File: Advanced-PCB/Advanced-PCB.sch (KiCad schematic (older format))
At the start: 24 parts, among them J1 USB_mini_micro_B, SW1 MXSwitch, SW2 MXSwitch, SW3 MXSwitch, SW4 MXSwitch, U1 ATMEGA32U4, X1 16MHz

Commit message: First Row Added
First Row added to layout and keycaps labeled.
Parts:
- removed D2: D_Small, Diode_SMD:D_SOD-123, symbol Device:D_Small
- removed SW2: MXSwitch, acheron_MXH:MX100H, symbol acheronSymbols:MXSwitch
- added D10, D11, D12, D13, D14, D15, D3, D5, D6, D7, D8, D9: 1N4148W, Diode_SMD:D_SOD-123, symbol Device:D_Small
- added SW10: 9, acheron_MXH:MX100H, symbol acheronSymbols:MXSwitch
- added SW11: 0, acheron_MXH:MX100H, symbol acheronSymbols:MXSwitch
- added SW12: -, acheron_MXH:MX100H, symbol acheronSymbols:MXSwitch
- added SW13: =, acheron_MXH:MX100H, symbol acheronSymbols:MXSwitch
- added SW14: Back, acheron_MXH:MX100H, symbol acheronSymbols:MXSwitch
- added SW15: `, acheron_MXH:MX100H, symbol acheronSymbols:MXSwitch
- added SW3: 2, acheron_MXH:MX100H, symbol acheronSymbols:MXSwitch
- added SW5: 4, acheron_MXH:MX100H, symbol acheronSymbols:MXSwitch
- added SW6: 5, acheron_MXH:MX100H, symbol acheronSymbols:MXSwitch
- added SW7: 6, acheron_MXH:MX100H, symbol acheronSymbols:MXSwitch
- added SW8: 7, acheron_MXH:MX100H, symbol acheronSymbols:MXSwitch
- added SW9: 8, acheron_MXH:MX100H, symbol acheronSymbols:MXSwitch
- D1, D4: value D_Small -> 1N4148W
- D2: renamed from D3; value D_Small -> 1N4148W
- SW1: value MXSwitch -> Esc
- SW2: renamed from SW3; value MXSwitch -> 1
- SW4: value MXSwitch -> 3
- renumbered C3 to C1, C1 to C2, C4 to C3, C5 to C4, C6 to C5, C7 to C6, C2 to C7, R3 to R2, R4 to R3, R2 to R4
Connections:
- net labels added: Col10, Col11, Col12, Col13, Col14, Col15, Col3, Col4, Col5, Col6, Col7, Col8, Col9, Row4, Row5
- net labels removed: Row2
- wire segments 74 -> 146
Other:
- moved on the sheet: C1, C2, C3, C4, C5, C6, C7, C8, J1, R1, R2, R3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

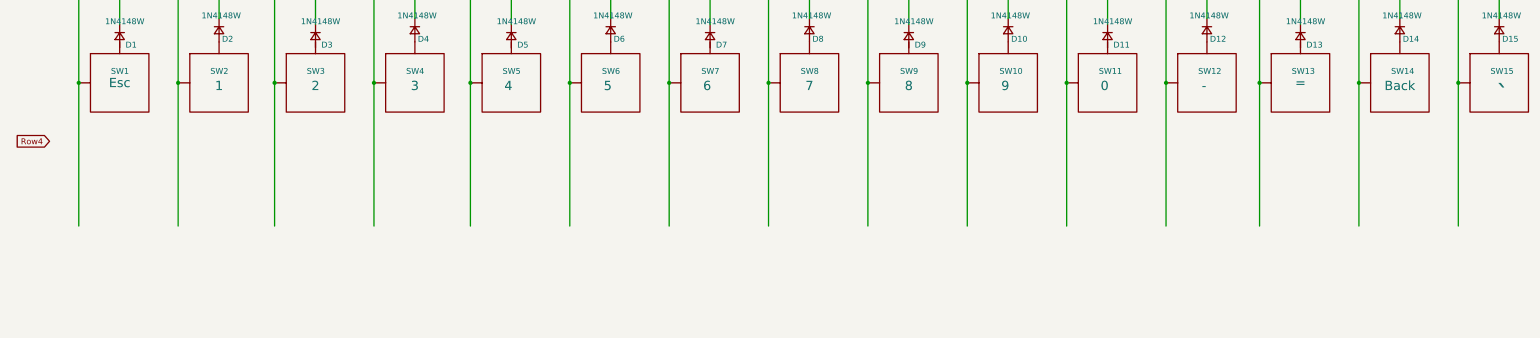
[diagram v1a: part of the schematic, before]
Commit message: Second Row Added
Second Row added to Matrix and Labeled.
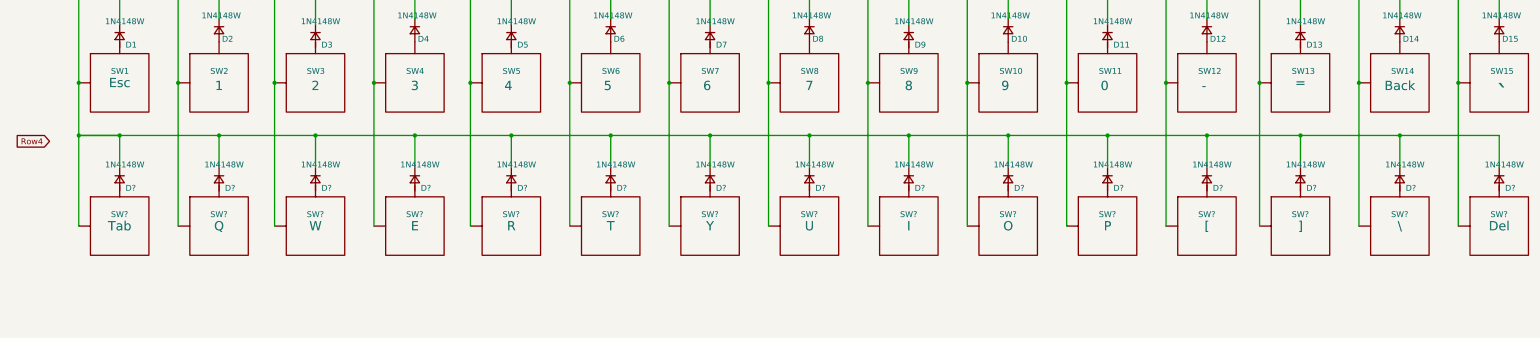
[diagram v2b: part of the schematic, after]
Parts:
- added D? (x15): 1N4148W, Diode_SMD:D_SOD-123, symbol Device:D_Small
- added SW?: Tab, acheron_MXH:MX100H, symbol acheronSymbols:MXSwitch
- added SW?: Q, acheron_MXH:MX100H, symbol acheronSymbols:MXSwitch
- added SW?: W, acheron_MXH:MX100H, symbol acheronSymbols:MXSwitch
- added SW?: E, acheron_MXH:MX100H, symbol acheronSymbols:MXSwitch
- added SW?: R, acheron_MXH:MX100H, symbol acheronSymbols:MXSwitch
- added SW?: T, acheron_MXH:MX100H, symbol acheronSymbols:MXSwitch
- added SW?: Y, acheron_MXH:MX100H, symbol acheronSymbols:MXSwitch
- added SW?: U, acheron_MXH:MX100H, symbol acheronSymbols:MXSwitch
- added SW?: I, acheron_MXH:MX100H, symbol acheronSymbols:MXSwitch
- added SW?: O, acheron_MXH:MX100H, symbol acheronSymbols:MXSwitch
- added SW?: P, acheron_MXH:MX100H, symbol acheronSymbols:MXSwitch
- added SW?: [, acheron_MXH:MX100H, symbol acheronSymbols:MXSwitch
- added SW?: ], acheron_MXH:MX100H, symbol acheronSymbols:MXSwitch
- added SW?: \\, acheron_MXH:MX100H, symbol acheronSymbols:MXSwitch
- added SW?: Del, acheron_MXH:MX100H, symbol acheronSymbols:MXSwitch
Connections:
- wire segments 146 -> 178

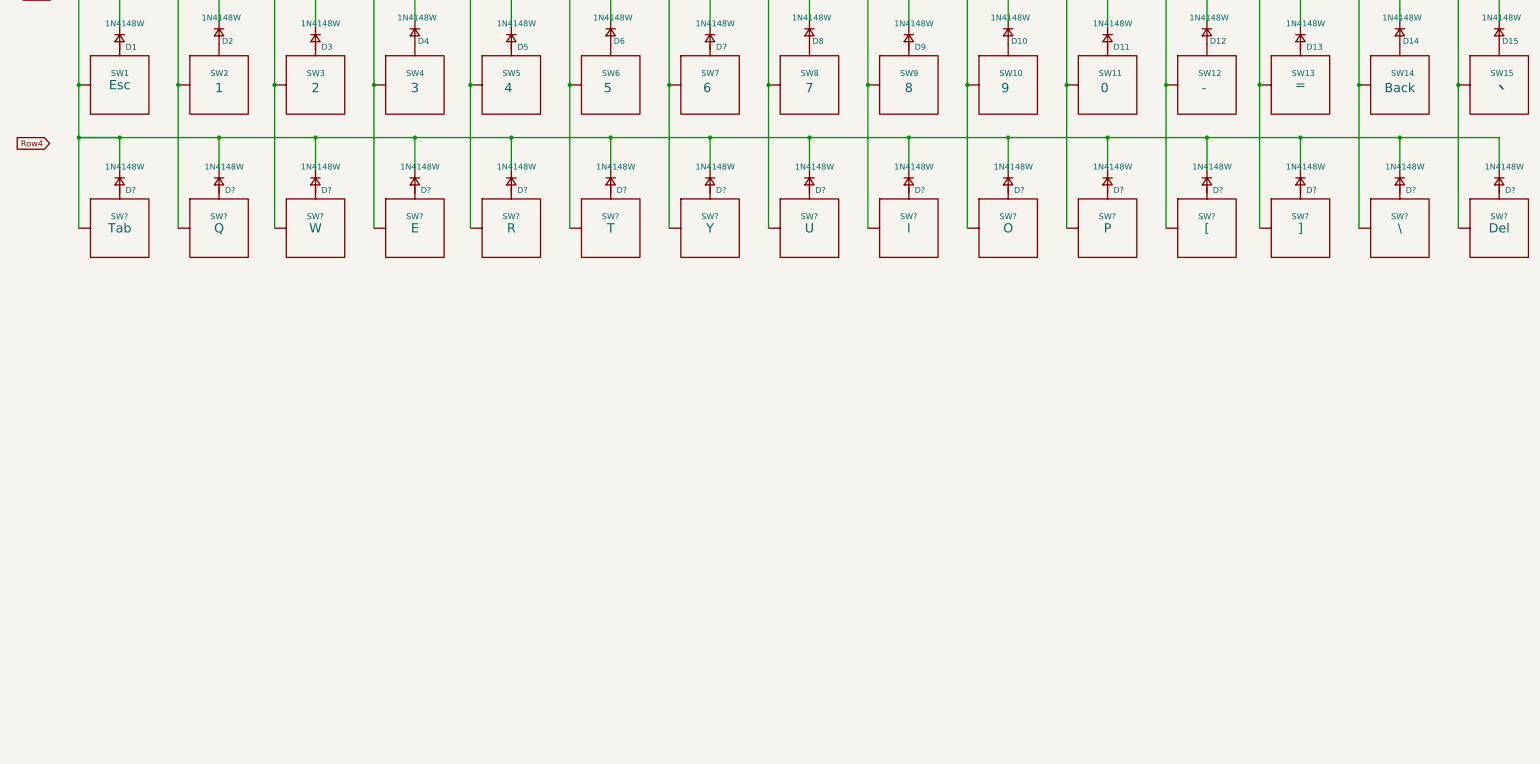
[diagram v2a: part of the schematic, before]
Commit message: KB Layout Finished
All KB rows and columns and labels added.
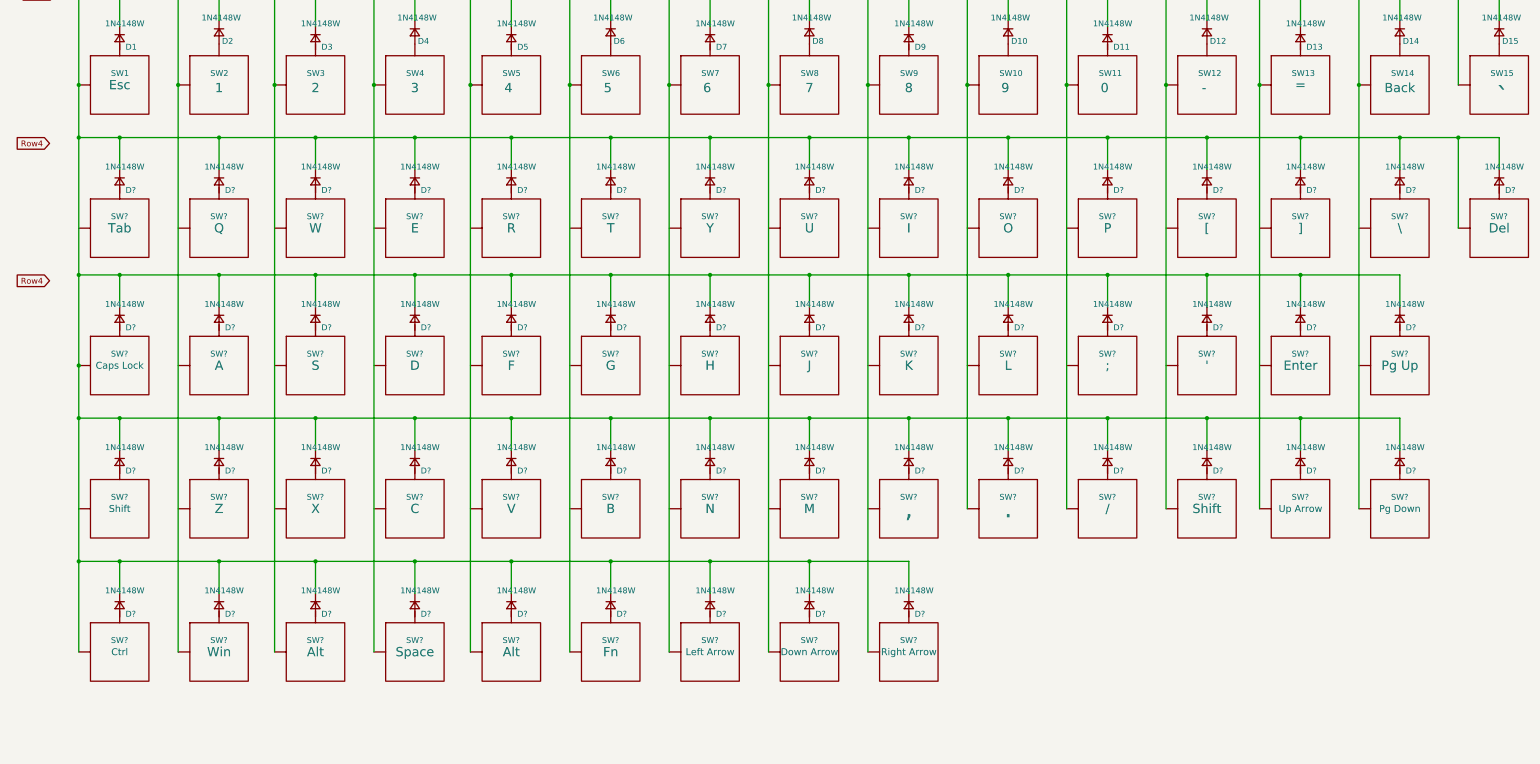
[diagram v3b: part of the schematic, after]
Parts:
- added D? (x37): 1N4148W, Diode_SMD:D_SOD-123, symbol Device:D_Small
- added SW?: Caps Lock, acheron_MXH:MX100H, symbol acheronSymbols:MXSwitch
- added SW?: A, acheron_MXH:MX100H, symbol acheronSymbols:MXSwitch
- added SW?: S, acheron_MXH:MX100H, symbol acheronSymbols:MXSwitch
- added SW?: D, acheron_MXH:MX100H, symbol acheronSymbols:MXSwitch
- added SW?: F, acheron_MXH:MX100H, symbol acheronSymbols:MXSwitch
- added SW?: G, acheron_MXH:MX100H, symbol acheronSymbols:MXSwitch
- added SW?: H, acheron_MXH:MX100H, symbol acheronSymbols:MXSwitch
- added SW?: J, acheron_MXH:MX100H, symbol acheronSymbols:MXSwitch
- added SW?: K, acheron_MXH:MX100H, symbol acheronSymbols:MXSwitch
- added SW?: L, acheron_MXH:MX100H, symbol acheronSymbols:MXSwitch
- added SW?: ;, acheron_MXH:MX100H, symbol acheronSymbols:MXSwitch
- added SW?: ', acheron_MXH:MX100H, symbol acheronSymbols:MXSwitch
- added SW?: Enter, acheron_MXH:MX100H, symbol acheronSymbols:MXSwitch
- added SW?: Pg Up, acheron_MXH:MX100H, symbol acheronSymbols:MXSwitch
- added SW? (x2): Shift, acheron_MXH:MX100H, symbol acheronSymbols:MXSwitch
- added SW?: Z, acheron_MXH:MX100H, symbol acheronSymbols:MXSwitch
- added SW?: X, acheron_MXH:MX100H, symbol acheronSymbols:MXSwitch
- added SW?: C, acheron_MXH:MX100H, symbol acheronSymbols:MXSwitch
- added SW?: V, acheron_MXH:MX100H, symbol acheronSymbols:MXSwitch
- added SW?: B, acheron_MXH:MX100H, symbol acheronSymbols:MXSwitch
- added SW?: N, acheron_MXH:MX100H, symbol acheronSymbols:MXSwitch
- added SW?: ,, acheron_MXH:MX100H, symbol acheronSymbols:MXSwitch
- added SW?: ., acheron_MXH:MX100H, symbol acheronSymbols:MXSwitch
- added SW?: /, acheron_MXH:MX100H, symbol acheronSymbols:MXSwitch
- added SW?: Up Arrow, acheron_MXH:MX100H, symbol acheronSymbols:MXSwitch
- added SW?: Pg Down, acheron_MXH:MX100H, symbol acheronSymbols:MXSwitch
- added SW?: M, acheron_MXH:MX100H, symbol acheronSymbols:MXSwitch
- added SW?: Ctrl, acheron_MXH:MX100H, symbol acheronSymbols:MXSwitch
- added SW?: Win, acheron_MXH:MX100H, symbol acheronSymbols:MXSwitch
- added SW? (x2): Alt, acheron_MXH:MX100H, symbol acheronSymbols:MXSwitch
- added SW?: Space, acheron_MXH:MX100H, symbol acheronSymbols:MXSwitch
- added SW?: Fn, acheron_MXH:MX100H, symbol acheronSymbols:MXSwitch
- added SW?: Left Arrow, acheron_MXH:MX100H, symbol acheronSymbols:MXSwitch
- added SW?: Right Arrow, acheron_MXH:MX100H, symbol acheronSymbols:MXSwitch
- added SW?: Down Arrow, acheron_MXH:MX100H, symbol acheronSymbols:MXSwitch
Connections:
- net Col1: now also D?.1 (K), D?.1 (K), D?.1 (K), D?.1 (K), D?.1 (K), D?.1 (K), D?.1 (K), D?.1 (K), D?.1 (K), D?.1 (K), D?.1 (K), D?.1 (K), D?.1 (K), D?.1 (K), D?.1 (K), D?.1 (K), D?.1 (K), D?.1 (K), D?.1 (K), D?.1 (K), D?.1 (K), D?.1 (K), D?.1 (K), D?.1 (K), D?.1 (K), D?.1 (K), D?.1 (K), D?.1 (K), D?.1 (K), D?.1 (K), D?.1 (K), D?.1 (K), D?.1 (K), D?.1 (K), D?.1 (K), D?.1 (K), D?.1 (K), SW?.1 (Col), SW?.1 (Col), SW?.1 (Col), SW?.1 (Col), SW?.1 (Col), SW?.1 (Col), SW?.1 (Col), SW?.1 (Col), SW?.1 (Col), SW?.1 (Col), SW?.1 (Col), SW?.1 (Col), SW?.1 (Col), SW?.1 (Col), SW?.1 (Col), SW?.1 (Col); no longer SW?.1 (Col), SW?.1 (Col), SW?.1 (Col), SW?.1 (Col), SW?.1 (Col), SW?.1 (Col), SW?.1 (Col), SW?.1 (Col), SW?.1 (Col), SW?.1 (Col), SW?.1 (Col), SW?.1 (Col), SW?.1 (Col), SW?.1 (Col)

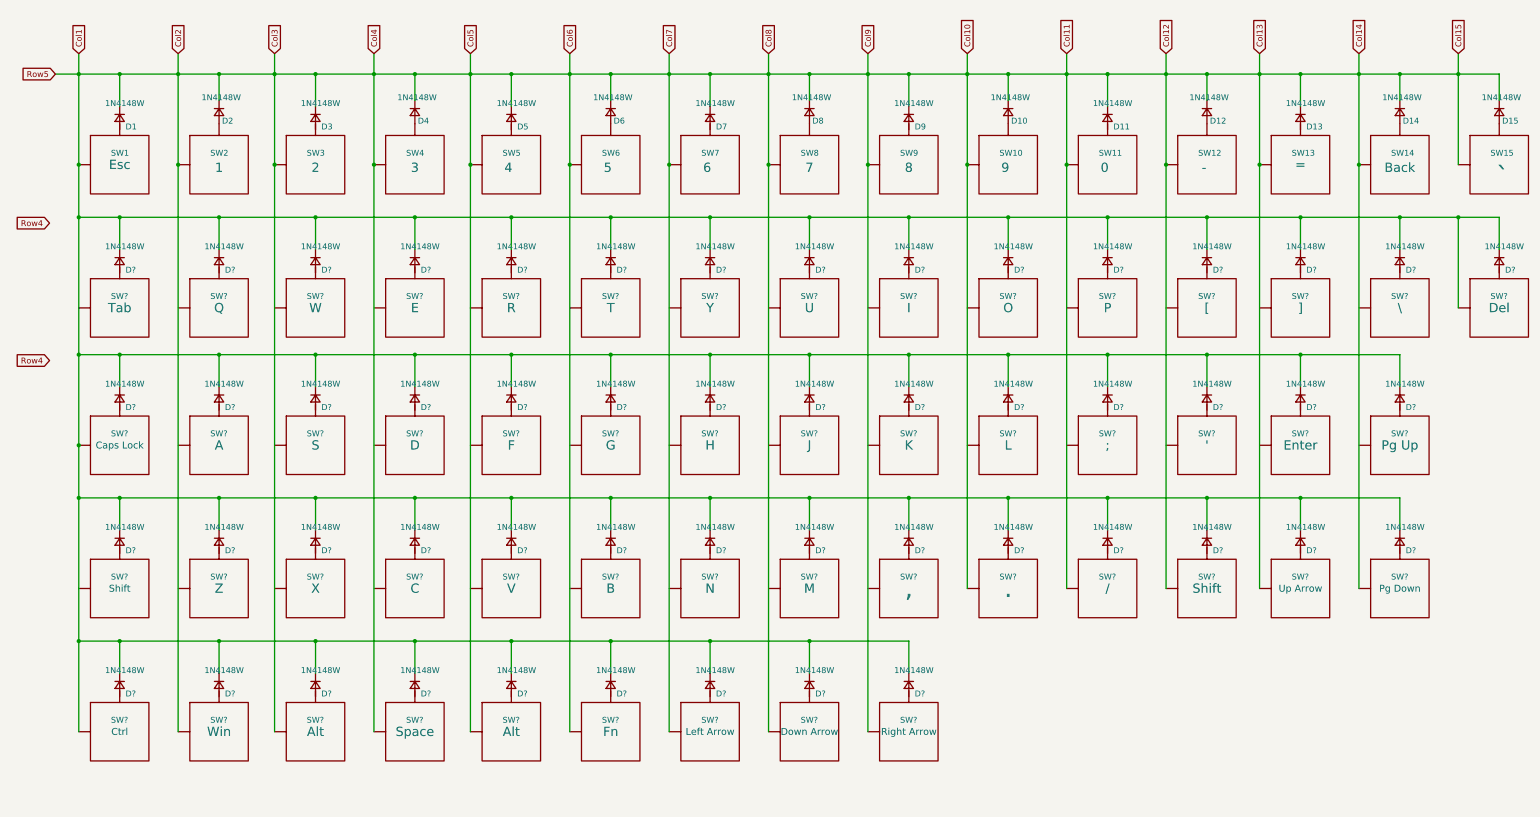
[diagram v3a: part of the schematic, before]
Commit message: Corrections and Fixes to Full Matrix
Full matrix completed and all wires and junctions connected properly, and all labels attached.
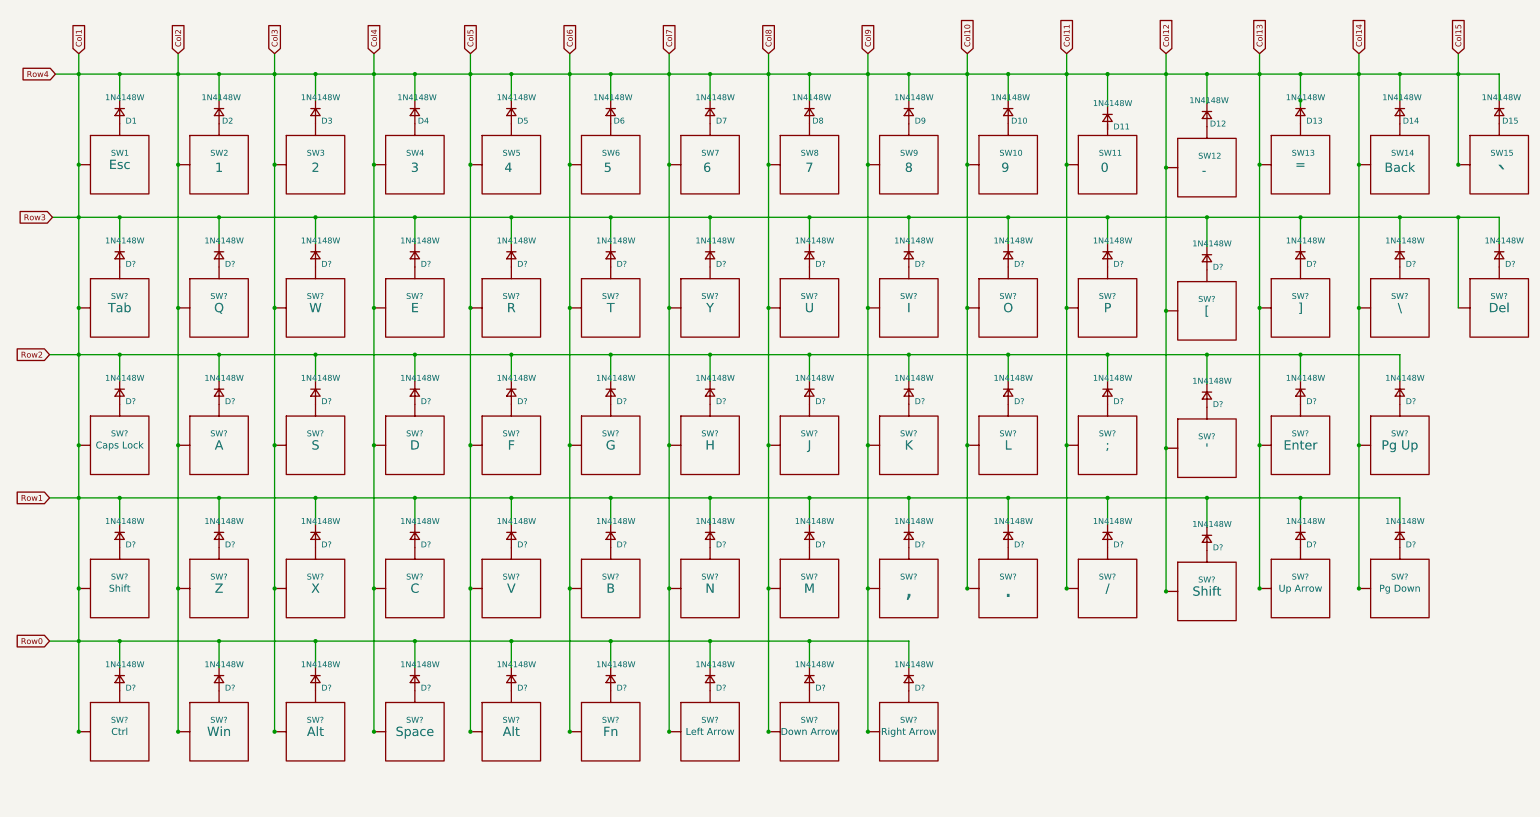
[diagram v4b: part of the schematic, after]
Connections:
- net Row1 is gone; now on net Col1: U1.40 (PF1), U1.41 (PF0)
- net Col1: now also SW?.1 (Col), SW?.1 (Col), SW?.1 (Col), SW?.1 (Col), SW?.1 (Col), SW?.1 (Col), SW?.1 (Col), SW?.1 (Col), SW?.1 (Col), SW?.1 (Col), SW?.1 (Col), SW?.1 (Col), SW?.1 (Col), SW?.1 (Col), SW?.1 (Col), SW?.1 (Col), SW?.1 (Col), SW?.1 (Col), SW?.1 (Col), SW?.1 (Col), SW?.1 (Col), SW?.1 (Col), SW?.1 (Col), SW?.1 (Col), SW?.1 (Col), SW?.1 (Col), SW?.1 (Col), SW?.1 (Col), SW?.1 (Col), SW?.1 (Col), SW?.1 (Col), SW?.1 (Col), SW?.1 (Col), SW?.1 (Col), SW?.1 (Col)
- net at SW1.2 (Row): now also D1.2 (A)
- net at D3.2 (A): now also SW3.2 (Row)
- net at D5.2 (A): now also SW5.2 (Row)
- net at D7.2 (A): now also SW7.2 (Row)
- net at D9.2 (A): now also SW9.2 (Row)
- net at D13.2 (A): now also SW13.2 (Row)
- net at D?.2 (A): now also SW?.2 (Row) (x52)
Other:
- moved on the sheet: D1, D12, D13, D3, D5, D7, D9, D?, SW12, SW?
